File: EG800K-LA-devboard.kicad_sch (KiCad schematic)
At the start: 48 parts, among them J1 U.FL-R-SMT_10_, J2 MICROQTJ, J5 Conn_01x08_Pin, Q1 DTC143ZUAT106, Q2 DTC143ZUAT106, Q4 DTC143ZUAT106, Q5 DTC143ZUAT106, Q6 BSS138, Q7 BSS138, Q8 BSS138, U4 EG800KEULC-I03-SNNSA

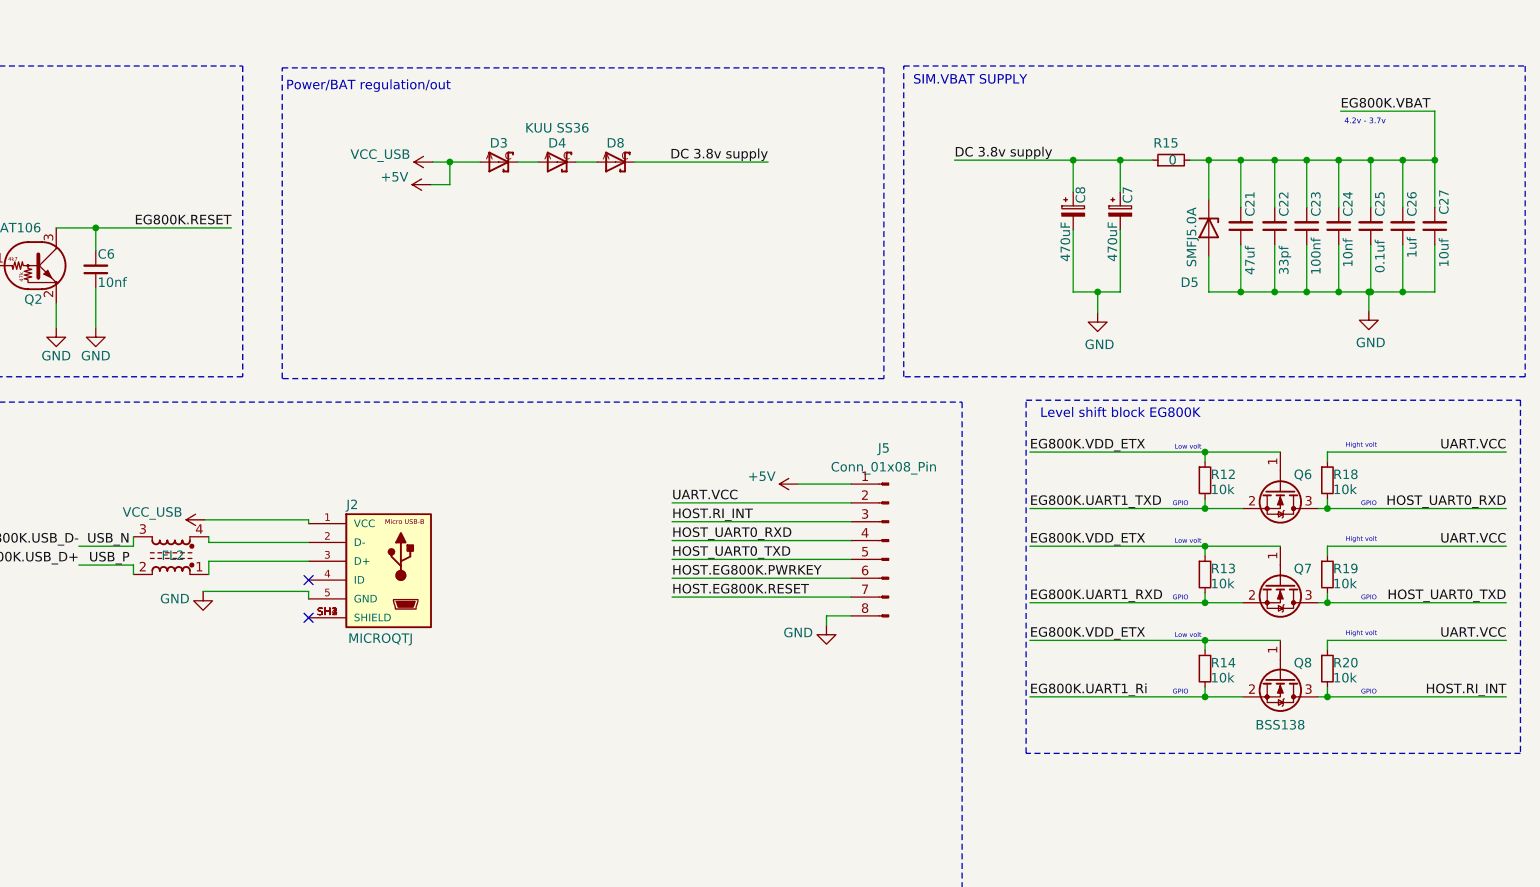
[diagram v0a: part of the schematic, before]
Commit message: cambio stack JLC PCB, cambio USB route
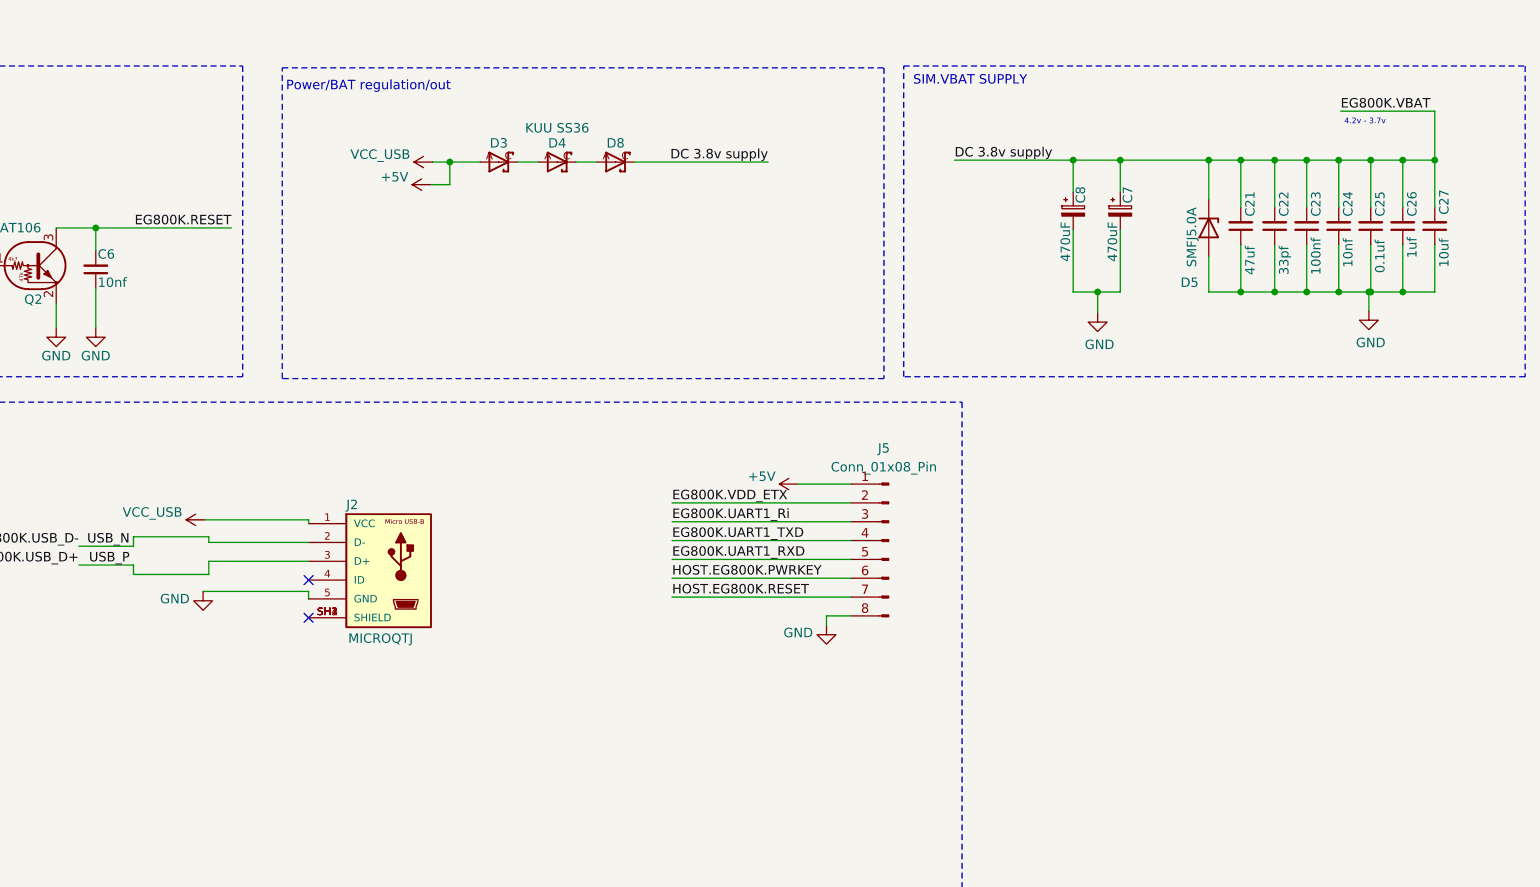
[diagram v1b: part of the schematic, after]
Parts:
- removed FL2: Choke_CommonMode_FerriteCore_1243, EasyEDA:FILTER-SMD_4P-L2.0-W1.2-BL_DLW21H, symbol Filter:Choke_CommonMode_FerriteCore_1243
- removed Q6, Q7, Q8: BSS138, Package_TO_SOT_SMD:SOT-23, symbol Transistor_FET:BSS138
- removed R12, R13, R14, R18, R19, R20: 10k, Resistor_SMD:R_0603_1608Metric_Pad0.98x0.95mm_HandSolder, symbol Device:R_Small
- removed R15: 0, Resistor_SMD:R_0603_1608Metric_Pad0.98x0.95mm_HandSolder, symbol Device:R_Small
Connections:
- net EG800K.VBAT is gone; now on net DC 3.8v supply: C21.2, C22.2, C23.2, C24.2, C25.2, C26.2, C27.2, D5.1 (K), D6.2 (A), D7.2 (A), U4.42 (VBAT), U4.43 (VBAT__1)
- net HOST.RI_INT is gone; now on net EG800K.UART1_Ri: J5.3 (Pin_3)
- net HOST_UART0_RXD is gone; now on net EG800K.UART1_TXD: J5.4 (Pin_4)
- net HOST_UART0_TXD is gone; now on net EG800K.UART1_RXD: J5.5 (Pin_5)
- net UART.VCC is gone; now on net EG800K.VDD_ETX: J5.2 (Pin_2)
- net EG800K.USB_D+: now also J2.3 (D+)
- net EG800K.USB_D-: now also J2.2 (D-)
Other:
- note removed: "GPIO"
- note removed: "Hight volt"
- note removed: "Level shift block EG800K"
- note removed: "Low volt"

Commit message: original rediseñado
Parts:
- removed J5: Conn_01x08_Pin, Connector_PinHeader_2.54mm:PinHeader_1x08_P2.54mm_Vertical, symbol Connector:Conn_01x08_Pin
- added BAT+1: BAT+, Connector_Wire:SolderWirePad_1x01_SMD_2x4mm, symbol Connector:Conn_01x01_Pin
- added BAT-1: BAT-, Connector_Wire:SolderWirePad_1x01_SMD_2x4mm, symbol Connector:Conn_01x01_Pin
- added J3: Conn_01x09_Pin, Connector_PinHeader_2.54mm:PinHeader_1x09_P2.54mm_Vertical, symbol Connector:Conn_01x09_Pin
- added Q3: AO3415, Package_TO_SOT_SMD:SOT-23, symbol Transistor_FET:AO3401A
- added R5: 2.4K, Resistor_SMD:R_0603_1608Metric_Pad0.98x0.95mm_HandSolder, symbol Device:R_Small
- added R6: 10k, Resistor_SMD:R_0603_1608Metric_Pad0.98x0.95mm_HandSolder, symbol Device:R_Small
- added U2: TP4057, Package_TO_SOT_SMD:TSOT-23-6, symbol Battery_Management:TP4057
- renumbered C22 to C10, C23 to C11, C24 to C12, C25 to C13, C26 to C14, C27 to C15, C4 to C3, C5 to C4, C3 to C5, C8 to C7, C7 to C8, C21 to C9, D3 to D2, D4 to D3, D8 to D4, R16 to R7, R17 to R8, U4 to U1
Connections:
- net +5V: now also J3.9 (Pin_9), Q3.1 (G), R6.1, U2.4 (V_{CC})
- net DC 3.8v supply: now also Q3.2 (S)
- net EG800K.UART1_RXD: now also J3.5 (Pin_5)
- net EG800K.UART1_Ri: now also J3.7 (Pin_7)
- net EG800K.UART1_TXD: now also J3.6 (Pin_6)
- net EG800K.VDD_ETX: now also J3.8 (Pin_8)
- net GND: now also BAT-1.1 (Pin_1), J3.1 (Pin_1), R5.2, R6.2, U2.2 (GND)
- net HOST.EG800K.PWRKEY: now also J3.4 (Pin_4)
- net HOST.EG800K.RESET: now also J3.3 (Pin_3)
- new net: R5.1, U2.6 (PROG)
- new net +4.2V: BAT+1.1 (Pin_1), J3.2 (Pin_2), Q3.3 (D), U2.3 (BAT)
- no-connect marks 20 -> 22
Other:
- note added: "500 mA"
- note added: "Bat"
- note added: "Bateria con sistema de proteccion"
- note added: "Coplanar Differential Pair Trace with: 0.2672 Impedance trace to copper 0.2032 Stackup: JLC04161H-7628"
- note added: "Coplanar Single Ended Trace with: 0.3424 Impedance trace to copper 0.5080 Stackup: JLC04161H-7628"
- note added: "P Mosfet conmutador DC/BAT"
- note added: "carga/descarga bateria"
- moved on the sheet: D2, D3, D4

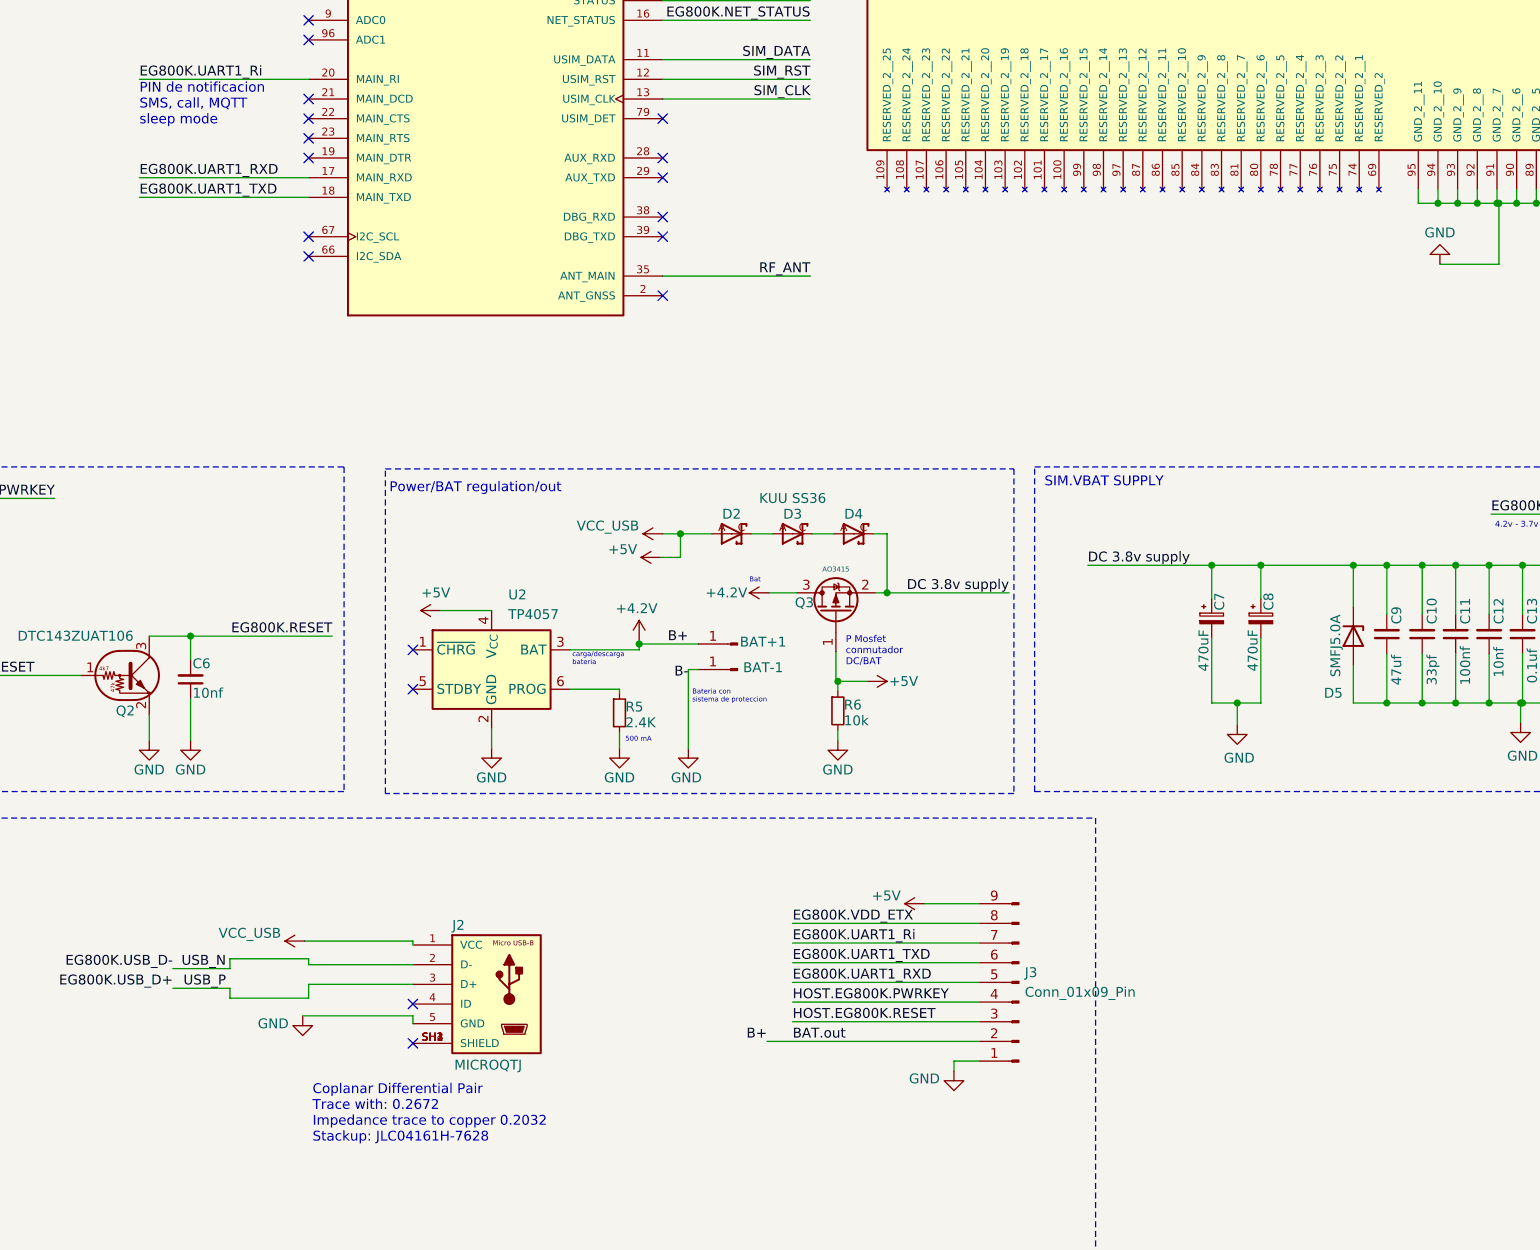
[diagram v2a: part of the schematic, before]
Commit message: agregado pin de vbat y detalles
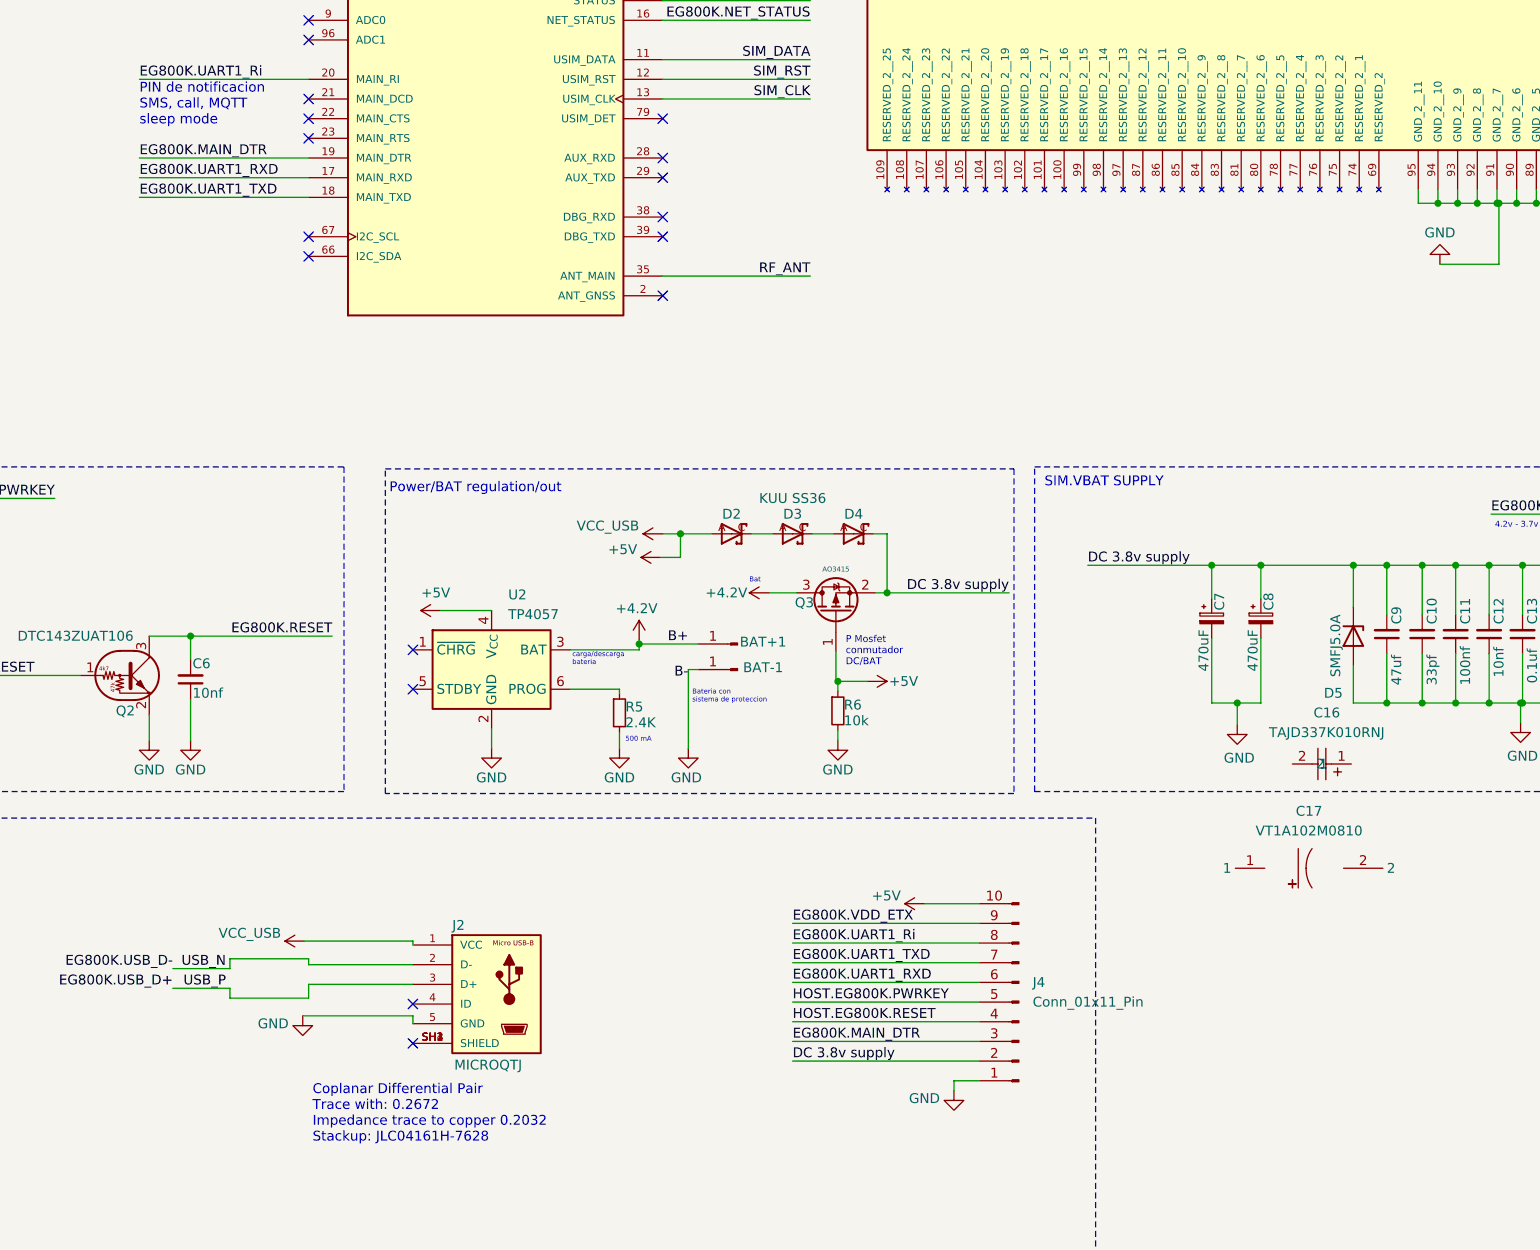
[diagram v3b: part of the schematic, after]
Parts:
- removed J3: Conn_01x09_Pin, Connector_PinHeader_2.54mm:PinHeader_1x09_P2.54mm_Vertical, symbol Connector:Conn_01x09_Pin
- added C16: TAJD337K010RNJ, EasyEDA:CASE-D_7343, symbol EasyEDA:TAJD337K010RNJ
- added C17: VT1A102M0810, EasyEDA:CAP-SMD_BD8.0-L8.3-W8.3-FD, symbol EasyEDA:VT1A102M0810
- added J4: Conn_01x11_Pin, Connector_PinHeader_2.54mm:PinHeader_1x10_P2.54mm_Vertical, symbol Connector:Conn_01x10_Pin
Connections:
- net +5V: now also J4.10 (Pin_10)
- net DC 3.8v supply: now also J4.2 (Pin_2)
- net EG800K.UART1_RXD: now also J4.6 (Pin_6)
- net EG800K.UART1_Ri: now also J4.8 (Pin_8)
- net EG800K.UART1_TXD: now also J4.7 (Pin_7)
- net EG800K.VDD_ETX: now also J4.9 (Pin_9)
- net GND: now also J4.1 (Pin_1)
- net HOST.EG800K.PWRKEY: now also J4.5 (Pin_5)
- net HOST.EG800K.RESET: now also J4.4 (Pin_4)
- net EG800K.MAIN_DTR: now reaches U1.19 (MAIN_DTR)
- net EG800K.MAIN_DTR: now also J4.3 (Pin_3)
- no-connect marks 22 -> 21

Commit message: carga final
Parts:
- removed BAT+1: BAT+, Connector_Wire:SolderWirePad_1x01_SMD_2x4mm, symbol Connector:Conn_01x01_Pin
- removed BAT-1: BAT-, Connector_Wire:SolderWirePad_1x01_SMD_2x4mm, symbol Connector:Conn_01x01_Pin
- removed C16: TAJD337K010RNJ, EasyEDA:CASE-D_7343, symbol EasyEDA:TAJD337K010RNJ
- removed C17: VT1A102M0810, EasyEDA:CAP-SMD_BD8.0-L8.3-W8.3-FD, symbol EasyEDA:VT1A102M0810
- added CN1: 530480210, EasyEDA:CONN-TH_530480210, symbol EasyEDA:530480210
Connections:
- net +4.2V: now also CN1.1
- net GND: now also CN1.2

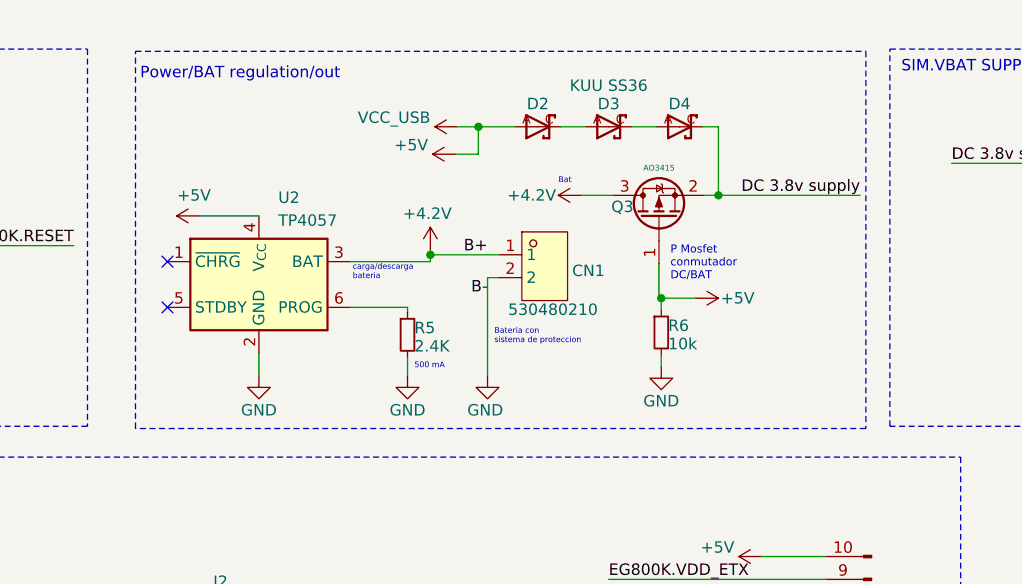
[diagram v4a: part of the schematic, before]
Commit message: removido la etapa de carga de BAT
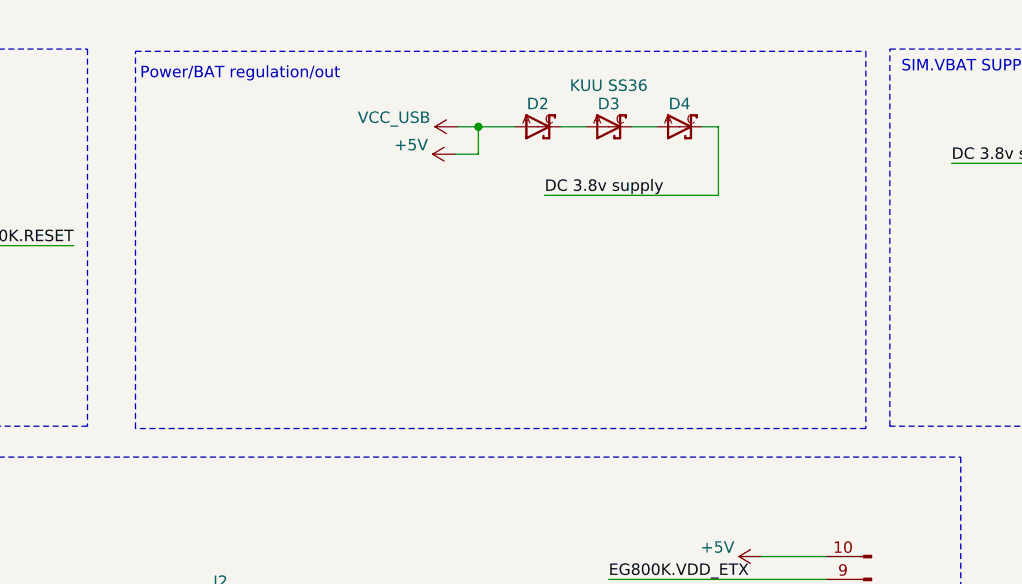
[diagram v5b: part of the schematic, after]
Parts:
- removed CN1: 530480210, EasyEDA:CONN-TH_530480210, symbol EasyEDA:530480210
- removed Q3: AO3415, Package_TO_SOT_SMD:SOT-23, symbol Transistor_FET:AO3401A
- removed R5: 2.4K, Resistor_SMD:R_0603_1608Metric_Pad0.98x0.95mm_HandSolder, symbol Device:R_Small
- removed R6: 10k, Resistor_SMD:R_0603_1608Metric_Pad0.98x0.95mm_HandSolder, symbol Device:R_Small
- removed U2: TP4057, Package_TO_SOT_SMD:TSOT-23-6, symbol Battery_Management:TP4057
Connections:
- no-connect marks 21 -> 19
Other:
- note removed: "500 mA"
- note removed: "Bat"
- note removed: "Bateria con sistema de proteccion"
- note removed: "P Mosfet conmutador DC/BAT"
- note removed: "carga/descarga bateria"
